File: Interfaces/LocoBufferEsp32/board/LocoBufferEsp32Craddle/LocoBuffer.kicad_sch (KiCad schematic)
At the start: 24 parts, among them J1 Conn_01x04, SW1 SW_Push, U2 AMS1117-5.0, U5 ESP32-DevKitC

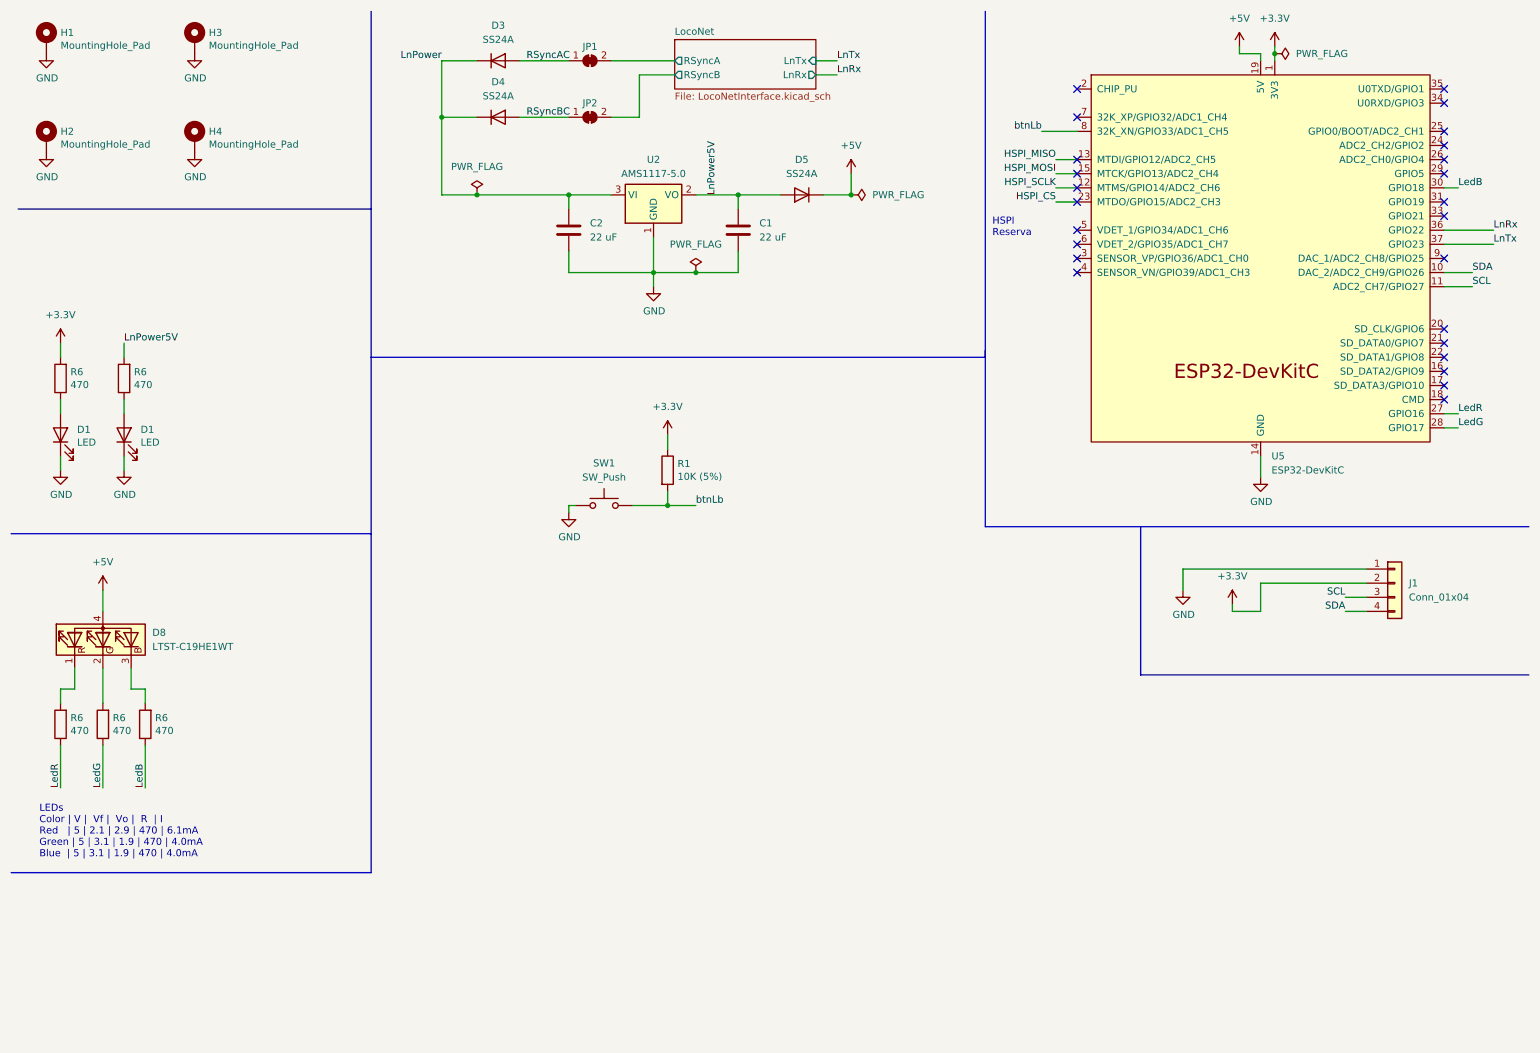
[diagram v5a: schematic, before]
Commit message: Buck converter
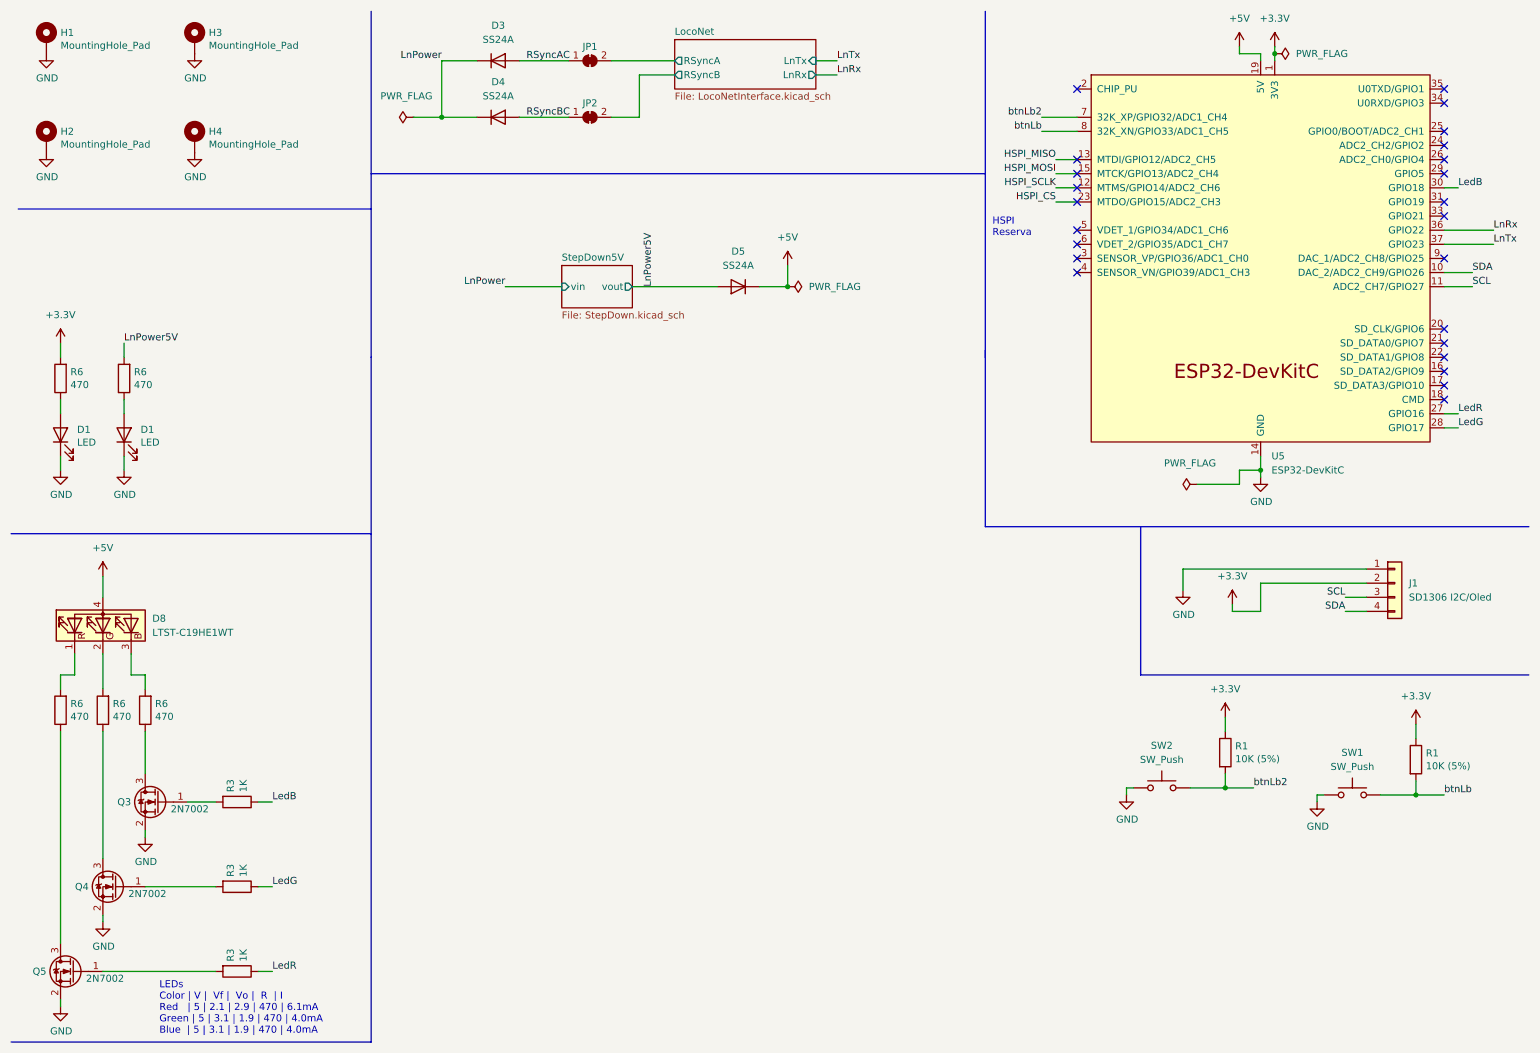
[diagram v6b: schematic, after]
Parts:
- removed C1, C2: 22 uF, Capacitor_SMD:C_1206_3216Metric, symbol Device:C
- removed U2: AMS1117-5.0, Package_TO_SOT_SMD:SOT-223-3_TabPin2, symbol Regulator_Linear:AMS1117-5.0
- added Q3, Q4, Q5: 2N7002, Package_TO_SOT_SMD:SOT-23, symbol Transistor_FET:2N7002
- added R1: 10K (5%), Resistor_SMD:R_0805_2012Metric, symbol Device:R
- added R3 (x3): 1K, Resistor_SMD:R_0805_2012Metric, symbol Device:R
- added SW2: SW_Push, Button_Switch_SMD:SW_SPST_CK_RS282G05A3, symbol Switch:SW_Push
- J1: value Conn_01x04 -> SD1306 I2C/Oled; footprint Connector_PinHeader_2.54mm:PinHeader_1x04_P2.54mm_Vertical -> LocoNetInterface:128x64OLED
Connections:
- net +3.3V: now also R1.1
- net GND: now also Q3.2 (S), Q4.2 (S), Q5.2 (S), SW2.1
- net LedB: now also R3.1; no longer R6.1
- net LedG: now also R3.1; no longer R6.1
- net LedR: now also R3.1; no longer R6.1
- net btnLb2: now reaches U5.7 (32K_XP/GPIO32/ADC1_CH4)
- net btnLb2: now also R1.2, SW2.2
- new net: Q4.1 (G), R3.2
- new net: Q3.3 (D), R6.1
- new net: Q3.1 (G), R3.2
- new net: Q5.3 (D), R6.1
- new net: Q4.3 (D), R6.1
- new net: Q5.1 (G), R3.2
- no-connect marks 25 -> 24
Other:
- added sheet StepDown5V (StepDown.kicad_sch)
- moved on the sheet: D5, D8, R1, R6, SW1
